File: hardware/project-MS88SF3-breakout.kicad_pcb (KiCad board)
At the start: 4 copper layers, 22.9 x 50.8 mm, 28 parts, among them J1 Conn_02x05_Odd_Even, J2 S2B-PH-SM4-TB(LF)(SN), J3 USB4105-GF-A, J4 Conn_01x12_Male, J5 Conn_01x16_Male, U1 MS88SF3_NRF52840

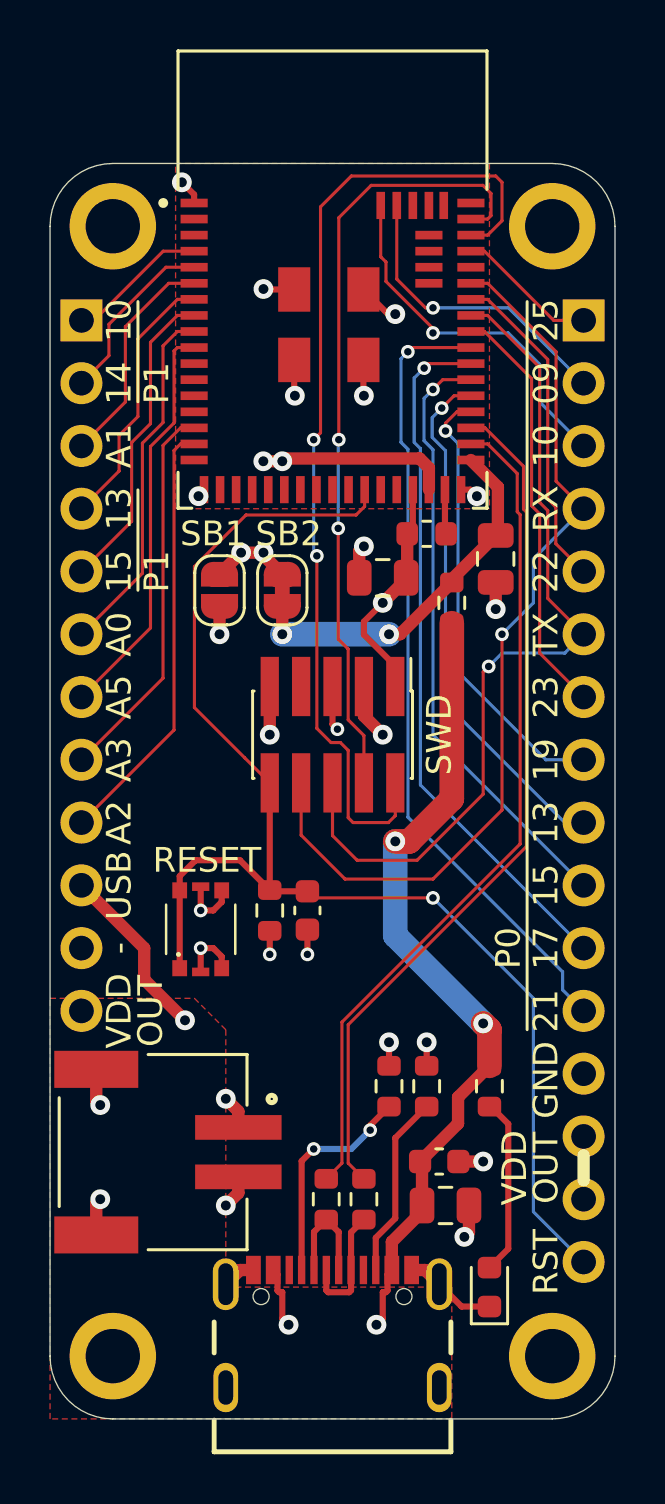
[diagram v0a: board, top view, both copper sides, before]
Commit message: Remove unused vias on VBUS fill
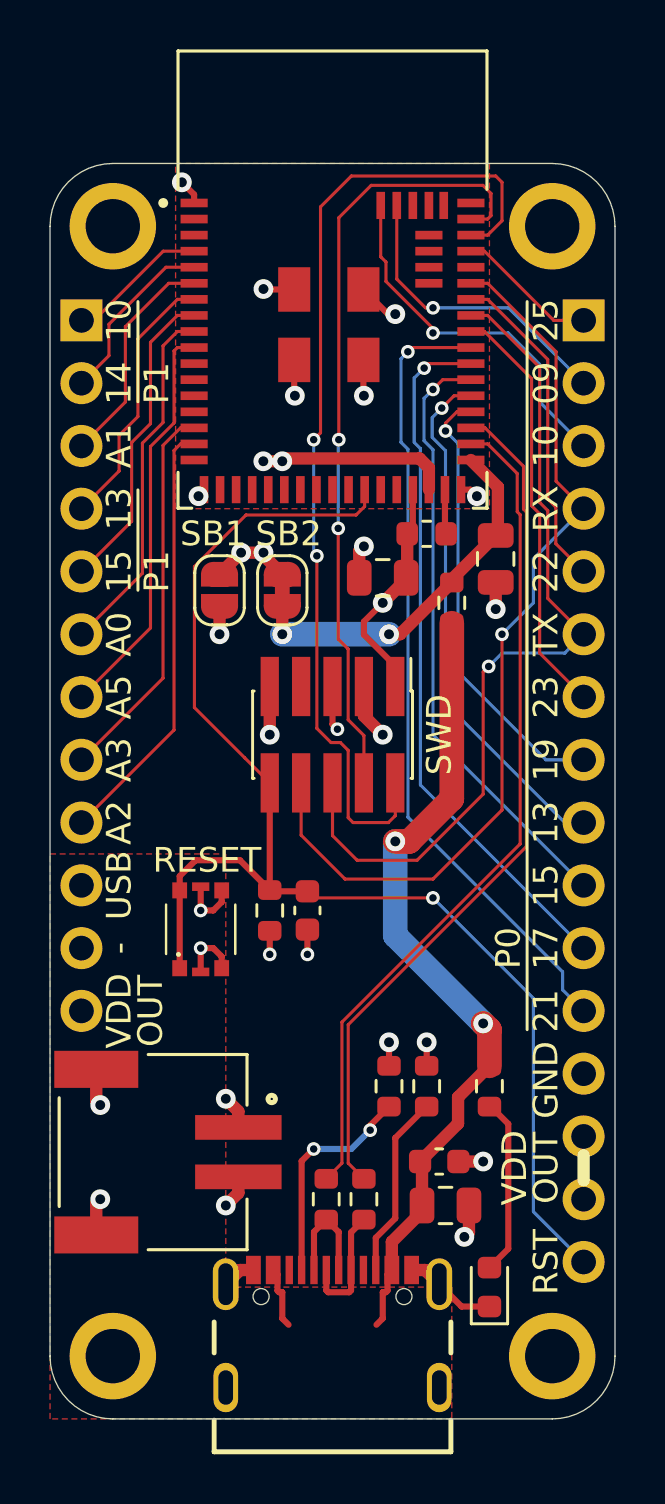
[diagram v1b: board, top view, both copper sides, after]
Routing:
- net /VBUS: track 43.0 -> 35.8 mm, vias 5 -> 2

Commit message: Remove version on silk
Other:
- board text added: "François Gervais 27 août 2022 v"
- board text removed: "François Gervais 27 août 2022 v1.0.0"
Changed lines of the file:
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@@
     (effects (font (size 1 1) (thickness 0.15)))
   )
-  (gr_text "François Gervais\n27 août 2022\nv1.0.0" (at 54.356 83.82) (layer B.SilkS)
+  (gr_text "François Gervais\n27 août 2022\nv" (at 54.356 83.82) (layer B.SilkS)
     (effects (font (size 1 1) (thickness 0.15)) (justify left mirror))
   )

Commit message: Upgrade ground fill under module
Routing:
- net GND: track 36.1 -> 29.5 mm
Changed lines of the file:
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@@
     (thickness 1.6)
     (drawings 53)
-    (tracks 396)
+    (tracks 386)
     (zones 0)
     (modules 28)
@@
     )
   )
-  (module MS88SF3_NRF52840:MODULE_MS88SF3_NRF52840 (layer F.Cu)
+  (module MS88SF3_NRF52840:MODULE_MS88SF3_NRF52840 locked (layer F.Cu)
     (at 47.498 85.471)
     (fp_text reference U1 (at -3.325 10.635) (layer F.Fab) hide
@@
     )
   )
-  (module Connector_PinHeader_2.54mm:PinHeader_1x12_P2.54mm_Vertical (layer B.Cu)
+  (module Connector_PinHeader_2.54mm:PinHeader_1x12_P2.54mm_Vertical locked (layer B.Cu)
     (at 37.338 87.122 180)
     (descr "Through hole straight pin header, 1x12, 2.54mm pitch, single row")
@@
     )
   )
-  (module USB4105-GF-A:GCT_USB4105-GF-A (layer F.Cu)
+  (module USB4105-GF-A:GCT_USB4105-GF-A locked (layer F.Cu)
     (at 47.498 130.302)
     (fp_text reference J3 (at -1.27 -6.858) (layer F.Fab) hide
@@
     )
   )
-  (module Connector_PinHeader_2.54mm:PinHeader_1x16_P2.54mm_Vertical (layer B.Cu)
+  (module Connector_PinHeader_2.54mm:PinHeader_1x16_P2.54mm_Vertical locked (layer B.Cu)
     (at 57.658 87.122 180)
     (descr "Through hole straight pin header, 1x16, 2.54mm pitch, single row")
@@
       (net 20 /RESET))
   )
-  (module "S2B-PH-SM4-TB(LF)(SN):JST_S2B-PH-SM4-TB(LF)(SN)" (layer F.Cu)
+  (module "S2B-PH-SM4-TB(LF)(SN):JST_S2B-PH-SM4-TB(LF)(SN)" locked (layer F.Cu)
     (at 43.688 120.777 270)
     (fp_text reference J2 (at -0.69228 -3.184 90) (layer F.Fab) hide
@@
     )
   )
-  (module MountingHole:MountingHole_2.2mm_M2_ISO7380_Pad (layer F.Cu)
+  (module MountingHole:MountingHole_2.2mm_M2_ISO7380_Pad locked (layer F.Cu)
     (at 56.388 83.312)
     (descr "Mounting Hole 2.2mm, M2, ISO7380")
@@
       (net 7 GND))
   )
-  (module MountingHole:MountingHole_2.2mm_M2_ISO7380_Pad (layer F.Cu)
+  (module MountingHole:MountingHole_2.2mm_M2_ISO7380_Pad locked (layer F.Cu)
     (at 38.608 83.312)
     (descr "Mounting Hole 2.2mm, M2, ISO7380")
@@
   (via (at 51.308 116.332) (size 0.8) (drill 0.4) (layers F.Cu B.Cu) (net 7))
   (segment (start 51.308 117.285) (end 51.308 116.332) (width 0.25) (layer F.Cu) (net 7))
-  (via (at 45.974 90.17) (size 0.8) (drill 0.4) (layers F.Cu B.Cu) (net 7))
-  (segment (start 45.948 88.721) (end 45.948 90.144) (width 0.25) (layer F.Cu) (net 7))
-  (segment (start 45.948 90.144) (end 45.974 90.17) (width 0.25) (layer F.Cu) (net 7))
-  (segment (start 52.698 93.971) (end 53.077 93.971) (width 0.25) (layer F.Cu) (net 7))
-  (via (at 53.34 94.234) (size 0.8) (drill 0.4) (layers F.Cu B.Cu) (net 7))
-  (segment (start 53.077 93.971) (end 53.34 94.234) (width 0.25) (layer F.Cu) (net 7))
   (segment (start 52.7215 127.0255) (end 51.818 126.122) (width 0.25) (layer F.Cu) (net 7))
   (segment (start 53.848 127.0255) (end 52.7215 127.0255) (width 0.25) (layer F.Cu) (net 7))
-  (via (at 42.075019 94.234) (size 0.8) (drill 0.4) (layers F.Cu B.Cu) (net 7))
-  (segment (start 42.298 93.971) (end 42.075019 94.193981) (width 0.25) (layer F.Cu) (net 7))
-  (segment (start 42.075019 94.193981) (end 42.075019 94.234) (width 0.25) (layer F.Cu) (net 7))
   (via (at 44.958 103.886) (size 0.8) (drill 0.4) (layers F.Cu B.Cu) (net 7))
   (segment (start 44.958 101.936) (end 44.958 103.886) (width 0.5) (layer F.Cu) (net 7))
@@
   (via (at 46.482 112.776) (size 0.554) (drill 0.3) (layers F.Cu B.Cu) (net 7))
   (segment (start 46.482 111.773) (end 46.482 112.776) (width 0.25) (layer F.Cu) (net 7))
-  (segment (start 48.748 88.721) (end 48.748 90.15) (width 0.25) (layer F.Cu) (net 7))
-  (via (at 48.768 90.17) (size 0.8) (drill 0.4) (layers F.Cu B.Cu) (net 7))
-  (segment (start 48.748 90.15) (end 48.768 90.17) (width 0.25) (layer F.Cu) (net 7))
-  (segment (start 44.723 85.871) (end 44.704 85.852) (width 0.25) (layer F.Cu) (net 7))
-  (segment (start 45.948 85.871) (end 44.723 85.871) (width 0.25) (layer F.Cu) (net 7))
-  (via (at 44.704 85.852) (size 0.8) (drill 0.4) (layers F.Cu B.Cu) (net 7))
-  (via (at 50.037976 86.868) (size 0.8) (drill 0.4) (layers F.Cu B.Cu) (net 7))
-  (segment (start 48.748 85.871) (end 49.745 86.868) (width 0.25) (layer F.Cu) (net 7))
-  (segment (start 49.745 86.868) (end 50.037976 86.868) (width 0.25) (layer F.Cu) (net 7))
-  (via (at 41.402014 81.534) (size 0.8) (drill 0.4) (layers F.Cu B.Cu) (net 7))
-  (segment (start 41.898 82.029986) (end 41.402014 81.534) (width 0.25) (layer F.Cu) (net 7))
-  (segment (start 41.898 82.371) (end 41.898 82.029986) (width 0.25) (layer F.Cu) (net 7))
+  (via (at 41.8846 81.4324) (size 0.8) (drill 0.4) (layers F.Cu B.Cu) (net 7))
+  (via (at 53.34 94.0816) (size 0.554) (drill 0.3) (layers F.Cu B.Cu) (net 7))
+  (segment (start 52.698 93.971) (end 53.2294 93.971) (width 0.25) (layer F.Cu) (net 7))
+  (segment (start 53.2294 93.971) (end 53.34 94.0816) (width 0.25) (layer F.Cu) (net 7))
+  (via (at 41.656 94.0816) (size 0.554) (drill 0.3) (layers F.Cu B.Cu) (net 7))
+  (segment (start 41.7666 93.971) (end 42.298 93.971) (width 0.25) (layer F.Cu) (net 7))
+  (segment (start 41.656 94.0816) (end 41.7666 93.971) (width 0.25) (layer F.Cu) (net 7))
+  (via (at 48.7426 84.1756) (size 0.8) (drill 0.4) (layers F.Cu B.Cu) (net 7))
+  (via (at 45.9486 84.1756) (size 0.8) (drill 0.4) (layers F.Cu B.Cu) (net 7))
+  (via (at 45.9486 90.424) (size 0.8) (drill 0.4) (layers F.Cu B.Cu) (net 7))
+  (via (at 48.7426 90.424) (size 0.8) (drill 0.4) (layers F.Cu B.Cu) (net 7))
   (segment (start 56.544499 88.390499) (end 56.544499 93.628499) (width 0.127) (layer F.Cu) (net 16))
   (segment (start 56.544499 93.628499) (end 57.658 94.742) (width 0.127) (layer F.Cu) (net 16))
@@
   (segment (start 41.348698 92.121) (end 41.898 92.121) (width 0.127) (layer F.Cu) (net 62))
   (segment (start 41.084499 92.385199) (end 41.348698 92.121) (width 0.127) (layer F.Cu) (net 62))
+  (segment (start 37.338 107.442) (end 41.084499 103.695501) (width 0.127) (layer F.Cu) (net 62))
   (segment (start 41.084499 103.695501) (end 41.084499 92.385199) (width 0.127) (layer F.Cu) (net 62))
-  (segment (start 37.338 107.442) (end 41.084499 103.695501) (width 0.127) (layer F.Cu) (net 62))
   (segment (start 41.348698 91.471) (end 41.898 91.471) (width 0.127) (layer F.Cu) (net 63))
   (segment (start 40.64 92.179698) (end 41.348698 91.471) (width 0.127) (layer F.Cu) (net 63))

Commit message: Open pcb and save
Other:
- net class Default removed
- net class Smallest removed
